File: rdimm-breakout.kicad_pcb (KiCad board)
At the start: 4 copper layers, 152.9 x 45 mm, 66 parts, among them IC1 MIC5317-2.5YM5-TR, J1 WE_629105150521, J4 0022232041, U1 FT2232HL-REEL, U14 2199155-1, U2 NCP163ASN330T1G, U8 PCA9517ADMR2G, Y1 KX-7_12,MHz

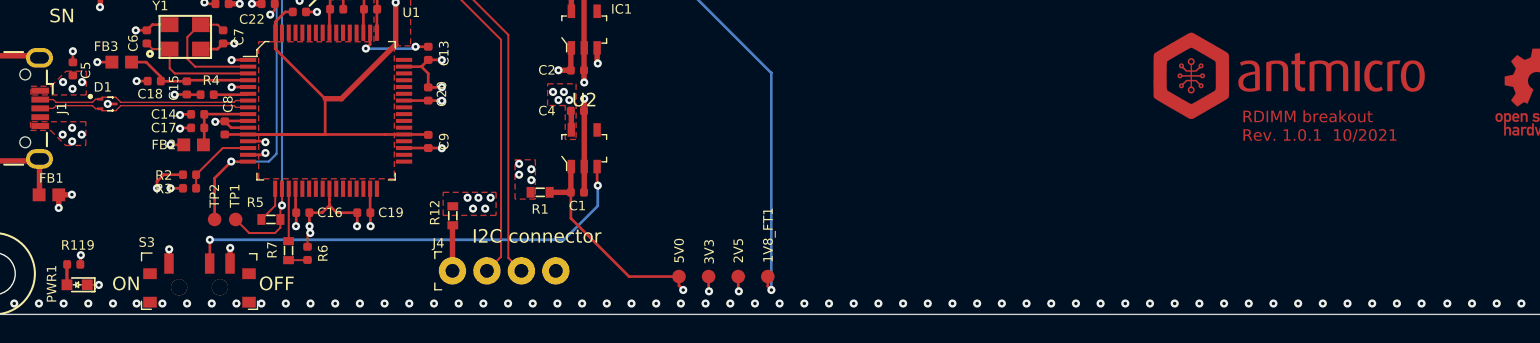
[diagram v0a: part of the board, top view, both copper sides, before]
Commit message: Fix 3V3 EN signal - bump rev. to 1.0.2
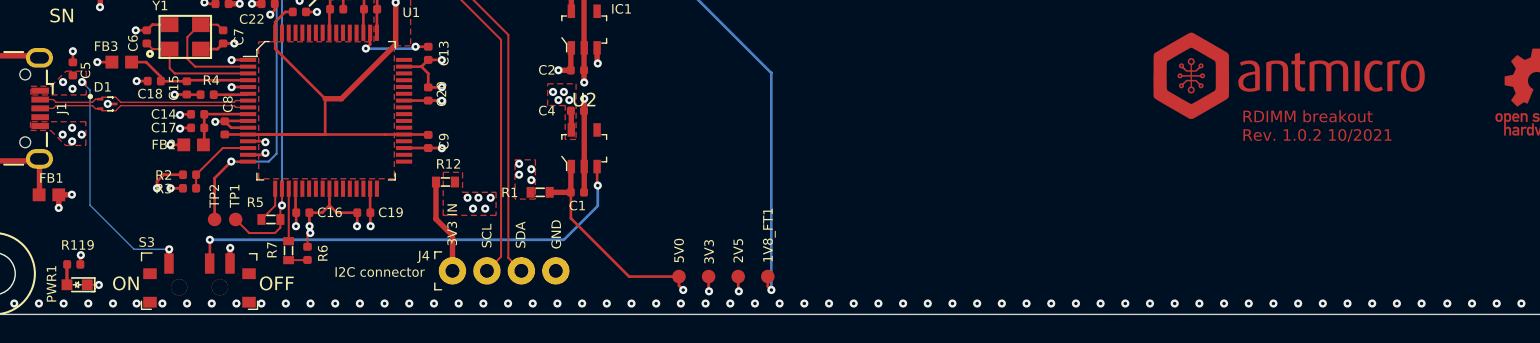
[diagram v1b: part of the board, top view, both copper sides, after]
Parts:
- moved R12 2.55 mm to (143.3, 81.2), turned to 180 degrees
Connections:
- J1 pad 4: Net-(J1-Pad4) -> (no net)
- S3 pad 1: VCC3V3 -> VBUS
- U1 pad 21: Net-(U1-Pad21) -> (no net)
- U1 pad 22: Net-(U1-Pad22) -> (no net)
- U1 pad 23: Net-(U1-Pad23) -> (no net)
- U1 pad 24: Net-(U1-Pad24) -> (no net)
- U1 pad 26: Net-(U1-Pad26) -> (no net)
- U1 pad 27: Net-(U1-Pad27) -> (no net)
- U1 pad 28: Net-(U1-Pad28) -> (no net)
- U1 pad 29: Net-(U1-Pad29) -> (no net)
- U1 pad 30: Net-(U1-Pad30) -> (no net)
- U1 pad 32: Net-(U1-Pad32) -> (no net)
- U1 pad 33: Net-(U1-Pad33) -> (no net)
- U1 pad 34: Net-(U1-Pad34) -> (no net)
- U1 pad 36: Net-(U1-Pad36) -> (no net)
- U1 pad 38: Net-(U1-Pad38) -> (no net)
- U1 pad 39: Net-(U1-Pad39) -> (no net)
- U1 pad 40: Net-(U1-Pad40) -> (no net)
- U1 pad 41: Net-(U1-Pad41) -> (no net)
- U1 pad 43: Net-(U1-Pad43) -> (no net)
- U1 pad 44: Net-(U1-Pad44) -> (no net)
- U1 pad 45: Net-(U1-Pad45) -> (no net)
- U1 pad 46: Net-(U1-Pad46) -> (no net)
- U1 pad 48: Net-(U1-Pad48) -> (no net)
- U1 pad 52: Net-(U1-Pad52) -> (no net)
- U1 pad 53: Net-(U1-Pad53) -> (no net)
- U1 pad 54: Net-(U1-Pad54) -> (no net)
- U1 pad 55: Net-(U1-Pad55) -> (no net)
- U1 pad 57: Net-(U1-Pad57) -> (no net)
- U1 pad 58: Net-(U1-Pad58) -> (no net)
- U1 pad 59: Net-(U1-Pad59) -> (no net)
- U1 pad 60: Net-(U1-Pad60) -> (no net)
- U1 pad 61: Net-(U1-Pad61) -> (no net)
- U1 pad 62: Net-(U1-Pad62) -> (no net)
- U1 pad 63: Net-(U1-Pad63) -> (no net)
- U14 pad 10: DQ6 -> (no net)
- U14 pad 100: DQS13_N -> (no net)
- U14 pad 102: DQ38 -> (no net)
- U14 pad 104: DQ34 -> (no net)
- U14 pad 106: DQ44 -> (no net)
- U14 pad 108: DQ40 -> (no net)
- U14 pad 110: DQS14_P -> (no net)
- U14 pad 111: DQS14_N -> (no net)
- U14 pad 113: DQ46 -> (no net)
- U14 pad 115: DQ42 -> (no net)
- U14 pad 117: DQ52 -> (no net)
- U14 pad 119: DQ48 -> (no net)
- U14 pad 12: DQ2 -> (no net)
- U14 pad 121: DQS15_P -> (no net)
- U14 pad 122: DQS15_N -> (no net)
- U14 pad 124: DQ54 -> (no net)
- U14 pad 126: DQ50 -> (no net)
- U14 pad 128: DQ60 -> (no net)
- U14 pad 130: DQ56 -> (no net)
- U14 pad 132: DQS16_P -> (no net)
- U14 pad 133: DQS16_N -> (no net)
- U14 pad 135: DQ62 -> (no net)
- U14 pad 137: DQ58 -> (no net)
- U14 pad 14: DQ12 -> (no net)
- U14 pad 144: Net-(U14-Pad144) -> (no net)
- U14 pad 146: VREFCA -> (no net)
- U14 pad 148: DQ5 -> (no net)
- U14 pad 150: DQ1 -> (no net)
- U14 pad 152: DQS0_N -> (no net)
- U14 pad 153: DQS0_P -> (no net)
- U14 pad 155: DQ7 -> (no net)
- U14 pad 157: DQ3 -> (no net)
- U14 pad 159: DQ13 -> (no net)
- U14 pad 16: DQ8 -> (no net)
- U14 pad 161: DQ9 -> (no net)
- U14 pad 163: DQS1_N -> (no net)
- U14 pad 164: DQS1_P -> (no net)
- U14 pad 166: DQ15 -> (no net)
- U14 pad 168: DQ11 -> (no net)
- U14 pad 170: DQ21 -> (no net)
- U14 pad 172: DQ17 -> (no net)
- U14 pad 174: DQS2_N -> (no net)
- U14 pad 175: DQS2_P -> (no net)
- U14 pad 177: DQ23 -> (no net)
- U14 pad 179: DQ19 -> (no net)
- U14 pad 18: DQS10_P -> (no net)
- U14 pad 181: DQ29 -> (no net)
- U14 pad 183: DQ25 -> (no net)
- U14 pad 185: DQS3_N -> (no net)
- U14 pad 186: DQS3_P -> (no net)
- U14 pad 188: DQ31 -> (no net)
- U14 pad 19: DQS10_N -> (no net)
- U14 pad 190: DQ27 -> (no net)
- U14 pad 192: CB5 -> (no net)
- U14 pad 194: CB1 -> (no net)
- U14 pad 196: DQS8_N -> (no net)
- U14 pad 197: DQS8_P -> (no net)
- U14 pad 199: CB7 -> (no net)
- U14 pad 201: CB3 -> (no net)
- U14 pad 203: CKE1\NC -> (no net)
- U14 pad 205: Net-(U14-Pad205) -> (no net)
- U14 pad 207: BG1 -> (no net)
- U14 pad 208: ~ALERT -> (no net)
- U14 pad 21: DQ14 -> (no net)
- U14 pad 210: A11 -> (no net)
- U14 pad 211: A7 -> (no net)
- U14 pad 213: A5 -> (no net)
- U14 pad 214: A4 -> (no net)
- U14 pad 216: A2 -> (no net)
- U14 pad 218: CK1_T -> (no net)
- U14 pad 219: CK1_C -> (no net)
- U14 pad 222: PARITY -> (no net)
- U14 pad 224: BA1 -> (no net)
- U14 pad 225: A10\AP -> (no net)
- U14 pad 227: Net-(U14-Pad227) -> (no net)
- U14 pad 228: ~WE~\A14 -> (no net)
- U14 pad 23: DQ10 -> (no net)
- U14 pad 230: ~SAVE -> (no net)
- U14 pad 232: A13 -> (no net)
- U14 pad 234: A17 -> (no net)
- U14 pad 235: NC\C2 -> (no net)
- U14 pad 237: ~CS3~\C1,NC -> (no net)
- U14 pad 240: DQ37 -> (no net)
- U14 pad 242: DQ33 -> (no net)
- U14 pad 244: DQS4_N -> (no net)
- U14 pad 245: DQS4_P -> (no net)
- U14 pad 247: DQ39 -> (no net)
- U14 pad 249: DQ35 -> (no net)
- U14 pad 25: DQ20 -> (no net)
- U14 pad 251: DQ45 -> (no net)
- U14 pad 253: DQ41 -> (no net)
- U14 pad 255: DQS5_N -> (no net)
- U14 pad 256: DQS5_P -> (no net)
- U14 pad 258: DQ47 -> (no net)
- U14 pad 260: DQ43 -> (no net)
- U14 pad 262: DQ53 -> (no net)
- U14 pad 264: DQ49 -> (no net)
- U14 pad 266: DQS6_N -> (no net)
- U14 pad 267: DQS6_P -> (no net)
- U14 pad 269: DQ55 -> (no net)
- U14 pad 27: DQ16 -> (no net)
- U14 pad 271: DQ51 -> (no net)
- U14 pad 273: DQ61 -> (no net)
- U14 pad 275: DQ57 -> (no net)
- U14 pad 277: DQS7_N -> (no net)
- U14 pad 278: DQS7_P -> (no net)
- U14 pad 280: DQ63 -> (no net)
- U14 pad 282: DQ59 -> (no net)
- U14 pad 29: DQS11_P -> (no net)
- U14 pad 3: DQ4 -> (no net)
- U14 pad 30: DQS11_N -> (no net)
- U14 pad 32: DQ22 -> (no net)
- U14 pad 34: DQ18 -> (no net)
- U14 pad 36: DQ28 -> (no net)
- U14 pad 38: DQ24 -> (no net)
- U14 pad 40: DQS12_P -> (no net)
- U14 pad 41: DQS12_N -> (no net)
- U14 pad 43: DQ30 -> (no net)
- U14 pad 45: DQ26 -> (no net)
- U14 pad 47: CB4 -> (no net)
- U14 pad 49: CB0 -> (no net)
- U14 pad 5: DQ0 -> (no net)
- U14 pad 51: DQS17_P -> (no net)
- U14 pad 52: DQS17_N -> (no net)
- U14 pad 54: CB6 -> (no net)
- U14 pad 56: CB2 -> (no net)
- U14 pad 58: ~RESET -> (no net)
- U14 pad 60: CKE0 -> (no net)
- U14 pad 62: ~ACT -> (no net)
- U14 pad 63: BG0 -> (no net)
- U14 pad 65: A12\~BC -> (no net)
- U14 pad 66: A9 -> (no net)
- U14 pad 68: A8 -> (no net)
- U14 pad 69: A6 -> (no net)
- U14 pad 7: DQS9_P -> (no net)
- U14 pad 71: A3 -> (no net)
- U14 pad 72: A1 -> (no net)
- U14 pad 74: CK0_T -> (no net)
- U14 pad 75: CK0_C -> (no net)
- U14 pad 79: A0 -> (no net)
- U14 pad 8: DQS9_N -> (no net)
- U14 pad 81: BA0 -> (no net)
- U14 pad 82: ~RAS~\A16 -> (no net)
- U14 pad 84: ~CS0 -> (no net)
- U14 pad 86: ~CAS~\A15 -> (no net)
- U14 pad 87: ODT0 -> (no net)
- U14 pad 89: ~CS1~\NC -> (no net)
- U14 pad 91: ODT1\NC -> (no net)
- U14 pad 93: ~CS2~\C0 -> (no net)
- U14 pad 95: DQ36 -> (no net)
- U14 pad 97: DQ32 -> (no net)
- U14 pad 99: DQS13_P -> (no net)
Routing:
- net VBUS: track 0.00 -> 17.9 mm, vias 7 -> 8
- net V_AUX: track 3.37 -> 7.05 mm
- net VCC3V3: track 34.5 -> 33.1 mm, vias 26 -> 25
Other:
- board text added: "3V3 IN"
- board text added: "GND"
- board text added: "RDIMM breakout Rev. 1.0.2 10/2021"
- board text added: "SCL"
- board text added: "SDA"
- board text removed: "RDIMM breakout Rev. 1.0.1 10/2021"
